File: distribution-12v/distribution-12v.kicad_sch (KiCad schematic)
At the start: 5 parts, among them J1 Conn_01x02_Socket, J3 Conn_01x02_Socket, J5 Conn_01x02_Socket

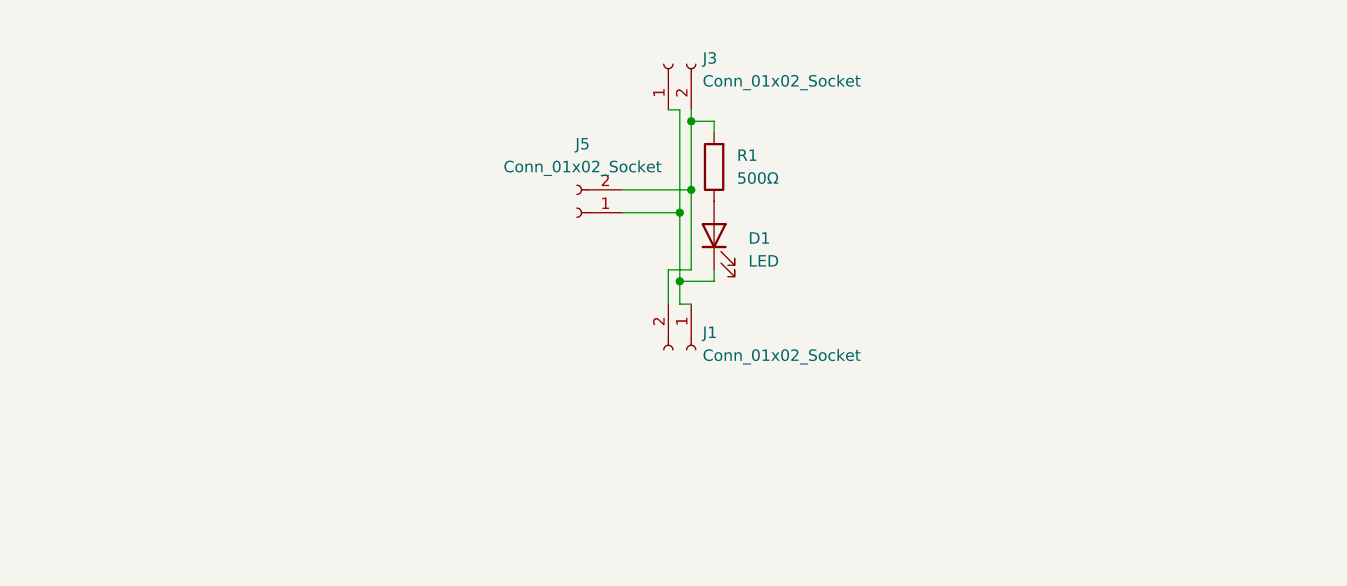
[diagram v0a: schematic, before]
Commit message: change: コネクタの数を3つに増やした
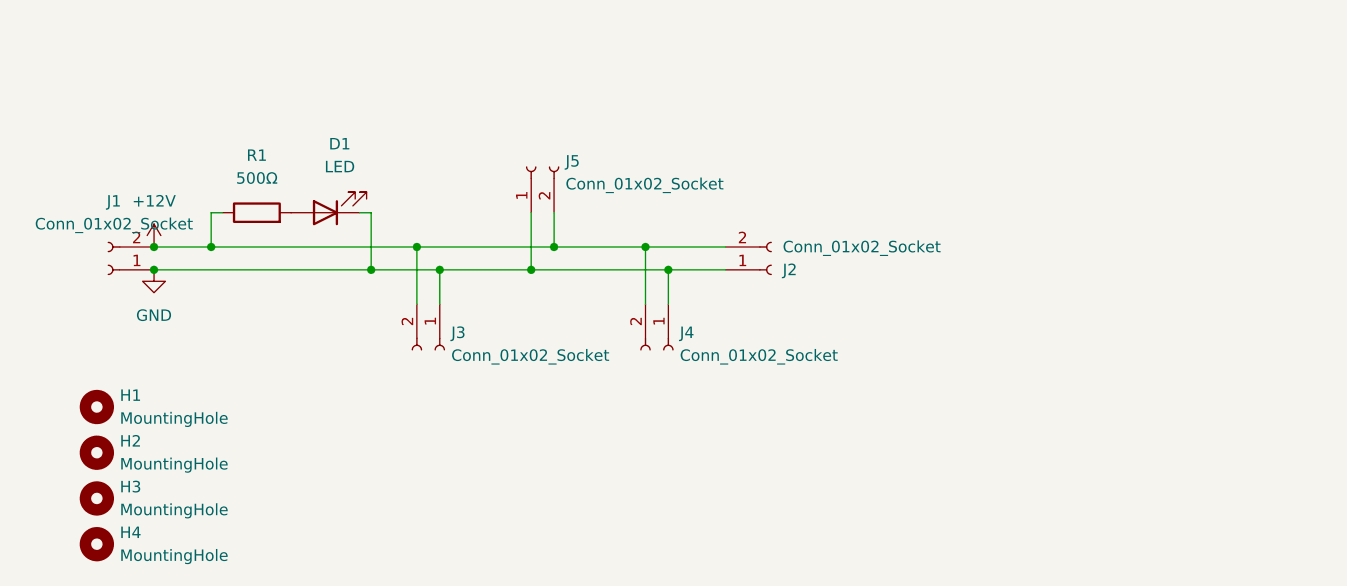
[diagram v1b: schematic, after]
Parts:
- added H1, H2, H3, H4: MountingHole, MountingHole:MountingHole_3.2mm_M3, symbol Mechanical:MountingHole
- added J2: Conn_01x02_Socket, Connector_AMASS:AMASS_XT60PW-F_1x02_P7.20mm_Horizontal, symbol Connector:Conn_01x02_Socket
- added J4: Conn_01x02_Socket, Connector_AMASS:AMASS_XT60-F_1x02_P7.20mm_Vertical, symbol Connector:Conn_01x02_Socket
- J1: footprint Connector_AMASS:AMASS_XT60PW-F_1x02_P7.20mm_Horizontal -> Connector_AMASS:AMASS_XT60PW-M_1x02_P7.20mm_Horizontal
- J3: footprint Connector_AMASS:AMASS_XT60PW-M_1x02_P7.20mm_Horizontal -> Connector_AMASS:AMASS_XT60-F_1x02_P7.20mm_Vertical
- R1: footprint Resistor_THT:R_Axial_DIN0207_L6.3mm_D2.5mm_P7.62mm_Horizontal -> Resistor_THT:R_Axial_DIN0207_L6.3mm_D2.5mm_P10.16mm_Horizontal
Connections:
- net GND: now reaches D1.1 (K), J1.1 (Pin_1), J3.1 (Pin_1), J5.1 (Pin_1)
- net GND: now also J2.1 (Pin_1), J4.1 (Pin_1)
- net +12V: now reaches J1.2 (Pin_2), J3.2 (Pin_2), J5.2 (Pin_2)
- net +12V: now also R1.1, J2.2 (Pin_2), J4.2 (Pin_2); no longer R1.2
- net at D1.2 (A): now also R1.2; no longer R1.1

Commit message: fix: まるごと作り直し
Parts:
- R1: footprint Resistor_THT:R_Axial_DIN0207_L6.3mm_D2.5mm_P10.16mm_Horizontal -> Resistor_THT:R_Axial_DIN0207_L6.3mm_D2.5mm_P7.62mm_Horizontal
